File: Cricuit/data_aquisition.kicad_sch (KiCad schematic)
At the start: 45 parts, among them J1 Raspberry_Pi_2_3, SW1 SW_SPST, SW10 SW_SPST, SW2 SW_SPST, SW3 SW_SPST, SW4 SW_SPST, SW5 SW_SPST, SW6 SW_SPST, SW7 SW_SPST, SW8 SW_SPST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

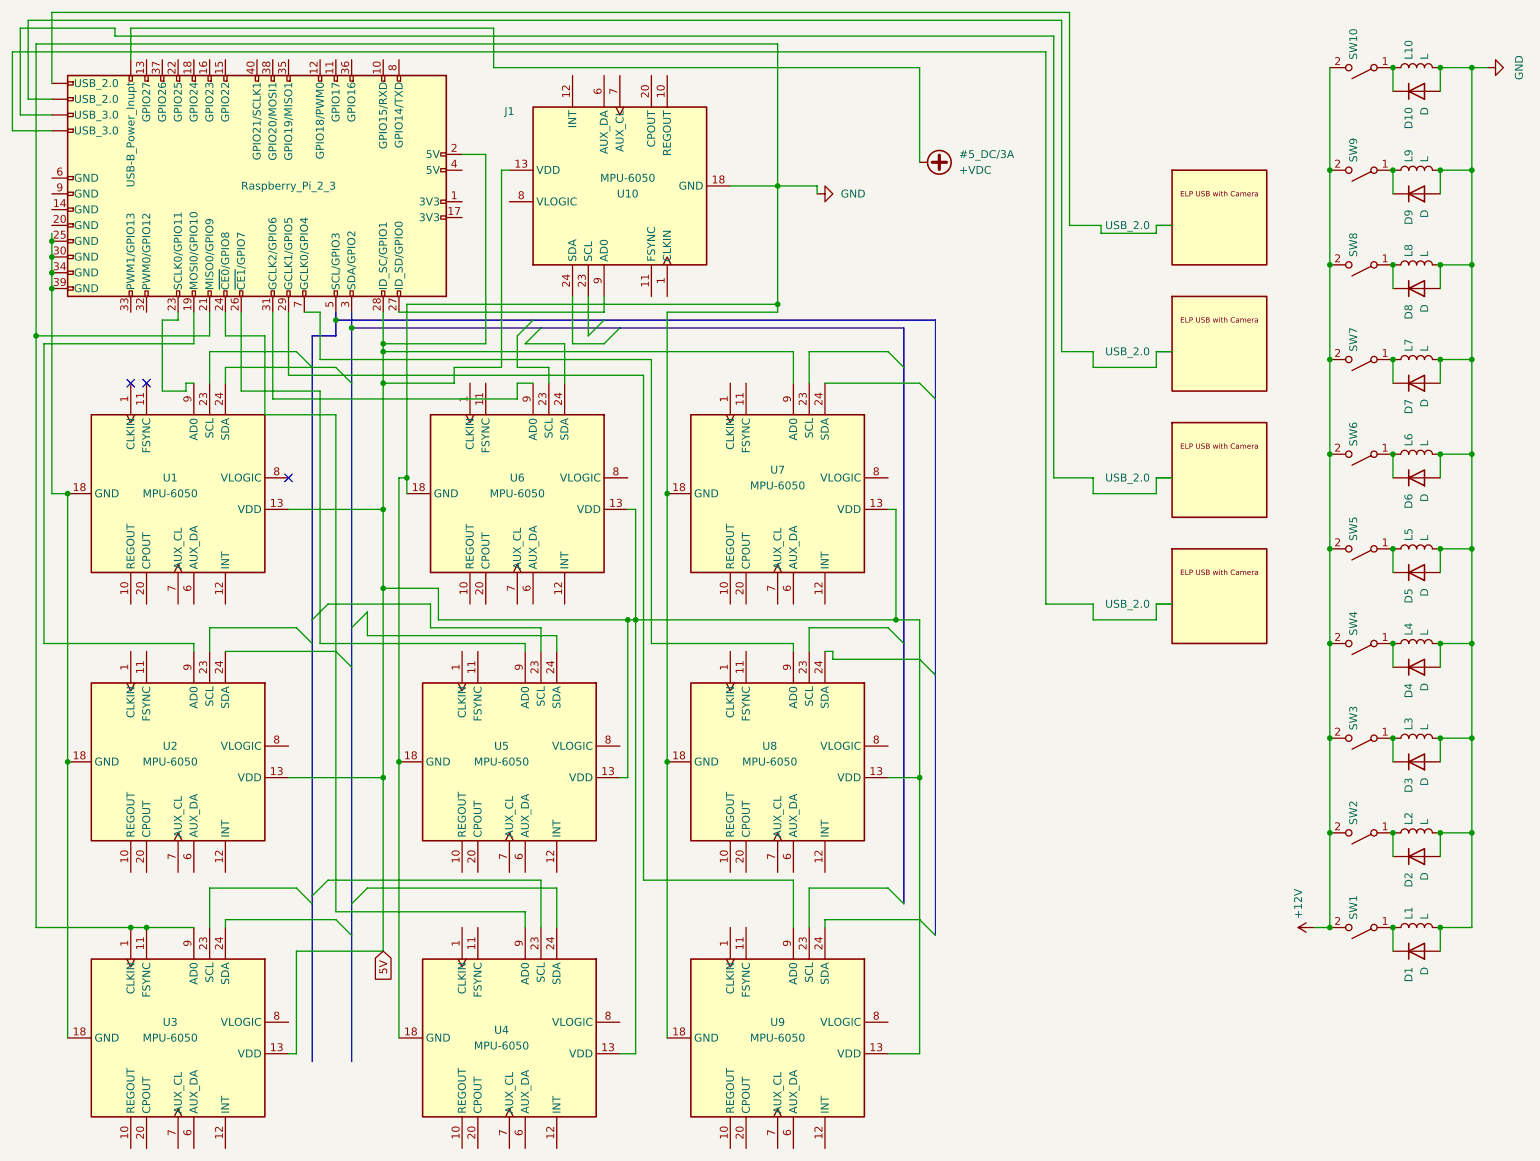
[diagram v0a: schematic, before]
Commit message: Reorganized the schematic
I chose arbitrary GPIO pins.
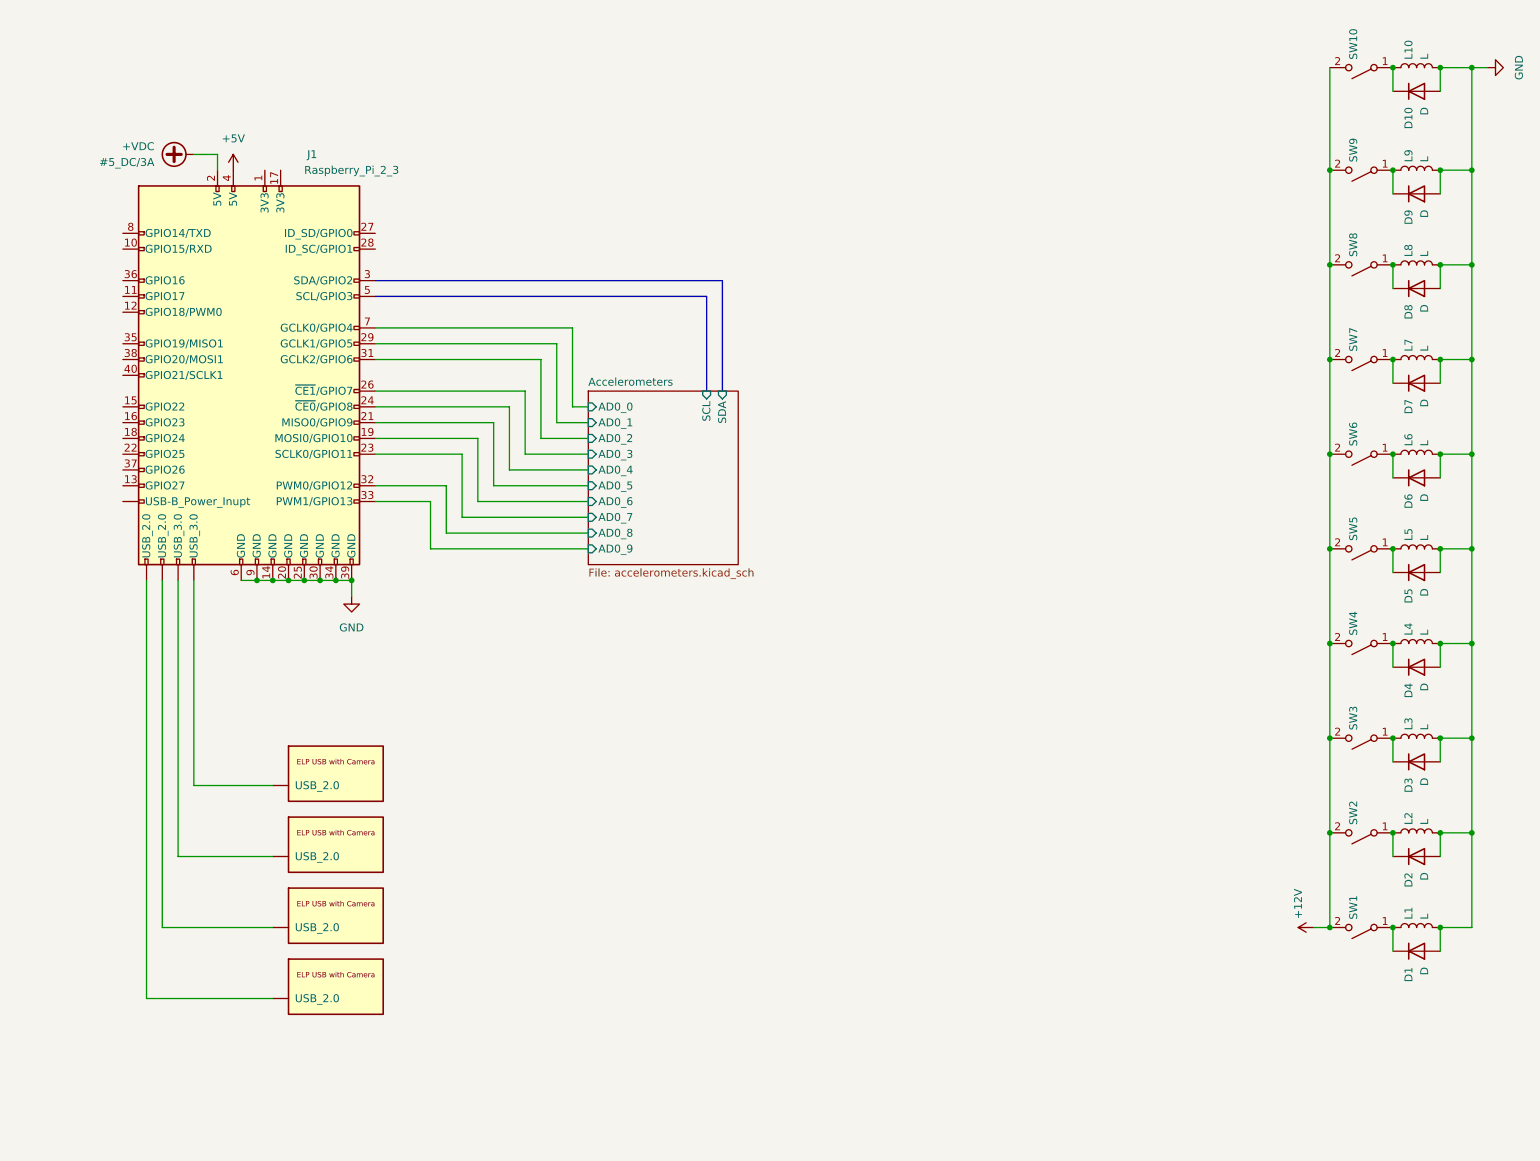
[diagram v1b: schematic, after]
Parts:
- removed U1, U10, U2, U3, U4, U5, U6, U7, U8, U9: MPU-6050, Sensor_Motion:InvenSense_QFN-24_4x4mm_P0.5mm, symbol Sensor_Motion:MPU-6050
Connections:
- net +VDC: now also J1.2 (5V); no longer J1. (USB_3.0)
- net GND: now also J1.14 (GND), J1.20 (GND), J1.25 (GND), J1.30 (GND), J1.34 (GND), J1.39 (GND), J1.6 (GND), J1.9 (GND); no longer J1.21 (MISO0/GPIO9)
- net Accelerometers/AD0_6: now reaches J1.19 (MOSI0/GPIO10)
- net Accelerometers/AD0_7: now reaches J1.23 (SCLK0/GPIO11)
- net Accelerometers/AD0_4: now reaches J1.24 (~{CE0}/GPIO8)
- net Accelerometers/AD0_3: now reaches J1.26 (~{CE1}/GPIO7)
- net Accelerometers/AD0_1: now reaches J1.29 (GCLK1/GPIO5)
- net Accelerometers/AD0_2: now reaches J1.31 (GCLK2/GPIO6)
- net Accelerometers/AD0_8: now reaches J1.32 (PWM0/GPIO12)
- net Accelerometers/AD0_9: now reaches J1.33 (PWM1/GPIO13)
- net +5V: now reaches J1.4 (5V)
- net Accelerometers/AD0_0: now reaches J1.7 (GCLK0/GPIO4)
- net 5V: no longer names the net of J1.28 (ID_SC/GPIO1)
- net 5V: no longer J1.2 (5V)
- new net Accelerometers/AD0_5: J1.21 (MISO0/GPIO9)
- no-connect marks 3 -> 0
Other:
- added sheet Accelerometers (accelerometers.kicad_sch)
- moved on the sheet: J1

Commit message: Small fix
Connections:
- net at J1. (USB_3.0): now also U14. (USB_2.0)

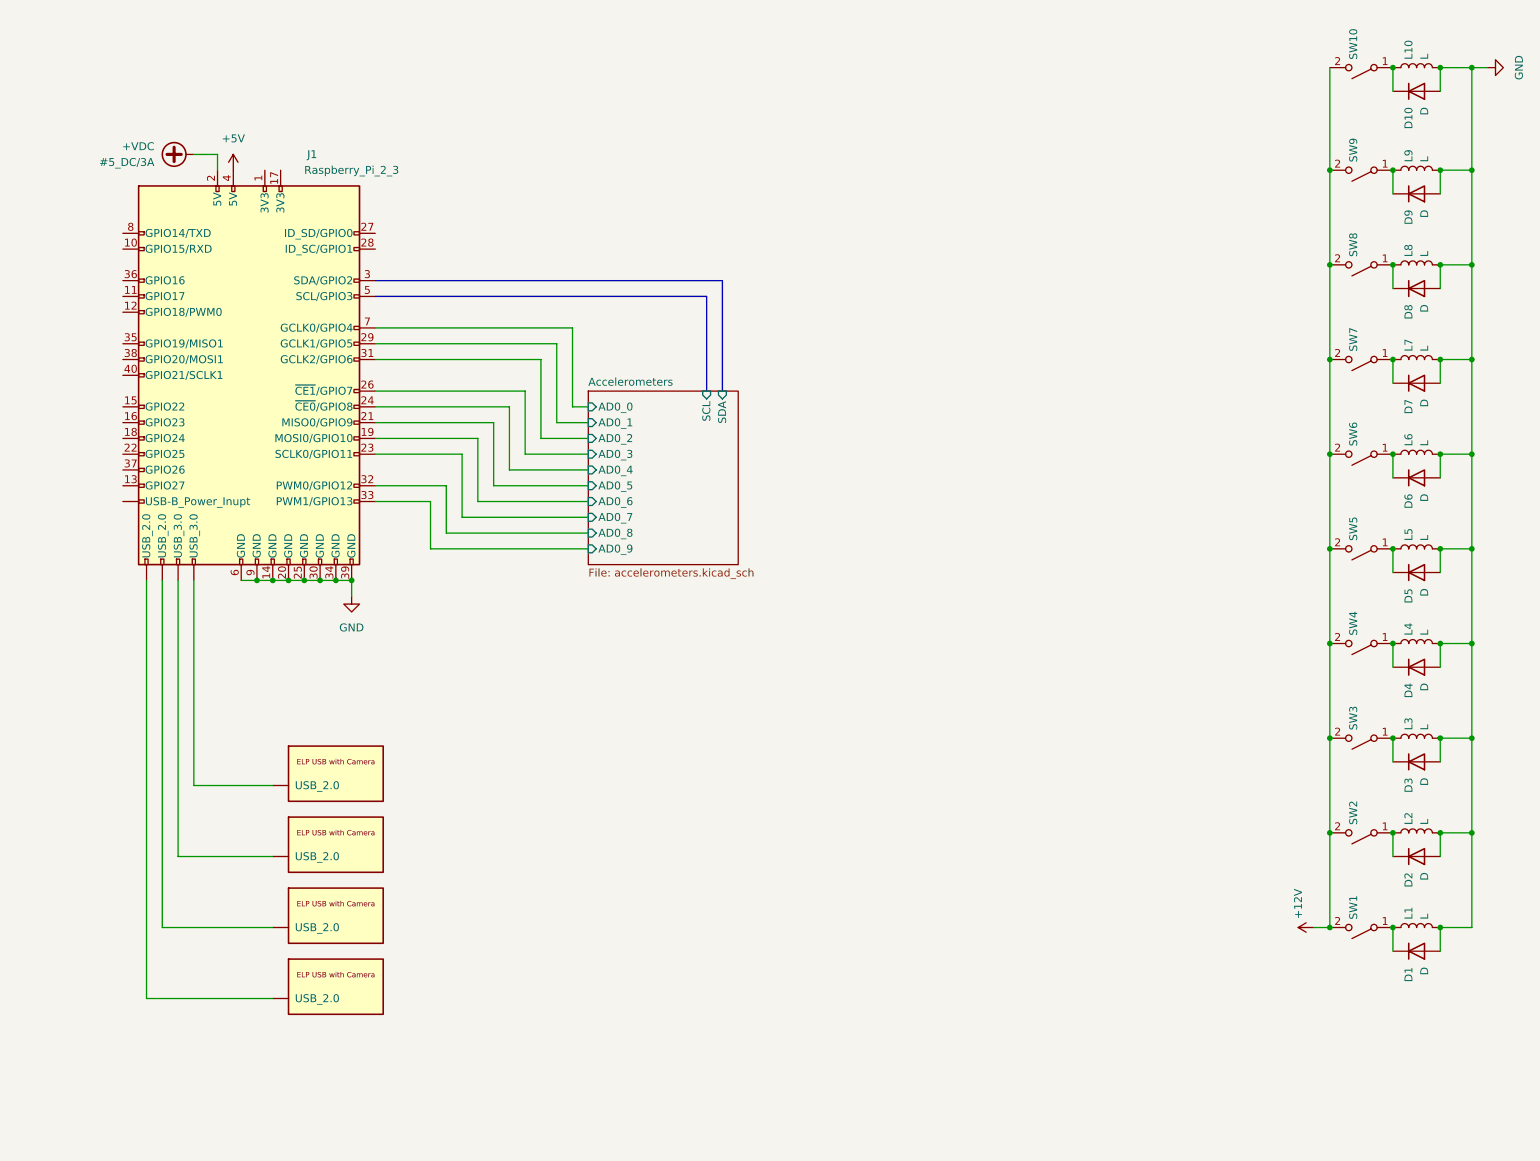
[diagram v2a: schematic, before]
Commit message: Added electromagnet subsheet
Now we have GPIO pin assignments for all components
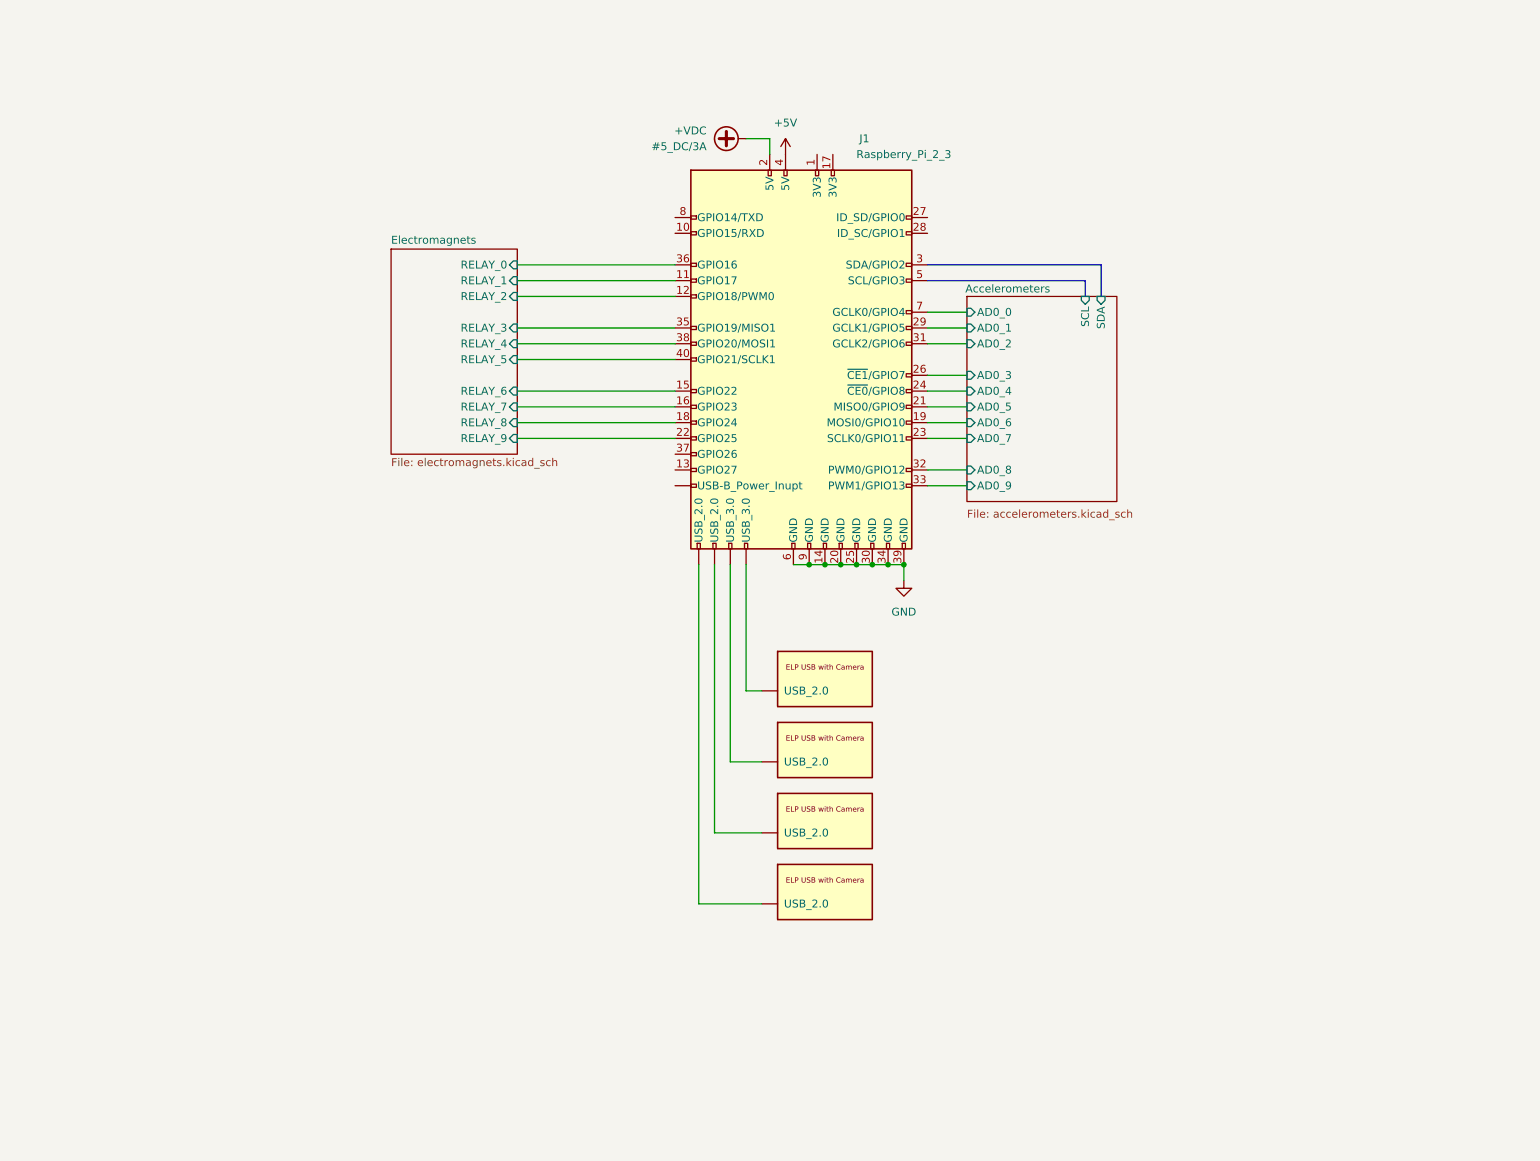
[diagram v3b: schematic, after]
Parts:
- removed D1, D10, D2, D3, D4, D5, D6, D7, D8, D9: D, symbol Device:D
- removed L1, L10, L2, L3, L4, L5, L6, L7, L8, L9: L, symbol Device:L
- removed SW1, SW10, SW2, SW3, SW4, SW5, SW6, SW7, SW8, SW9: SW_SPST, symbol Switch:SW_SPST
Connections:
- net at J1. (USB_3.0): now also U14. (USB_2.0)
- net Electromagnets/RELAY_1: now reaches J1.11 (GPIO17)
- net Electromagnets/RELAY_2: now reaches J1.12 (GPIO18/PWM0)
- net Electromagnets/RELAY_6: now reaches J1.15 (GPIO22)
- net Electromagnets/RELAY_7: now reaches J1.16 (GPIO23)
- net Electromagnets/RELAY_8: now reaches J1.18 (GPIO24)
- net Electromagnets/RELAY_9: now reaches J1.22 (GPIO25)
- net Electromagnets/RELAY_3: now reaches J1.35 (GPIO19/MISO1)
- net Electromagnets/RELAY_0: now reaches J1.36 (GPIO16)
- net Electromagnets/RELAY_4: now reaches J1.38 (GPIO20/MOSI1)
- net Electromagnets/RELAY_5: now reaches J1.40 (GPIO21/SCLK1)
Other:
- added sheet Electromagnets (electromagnets.kicad_sch)
- company: (none) -> CMD_SAT
- title: (none) -> Data Acquisition and Latching Circuits
- moved on the sheet: J1

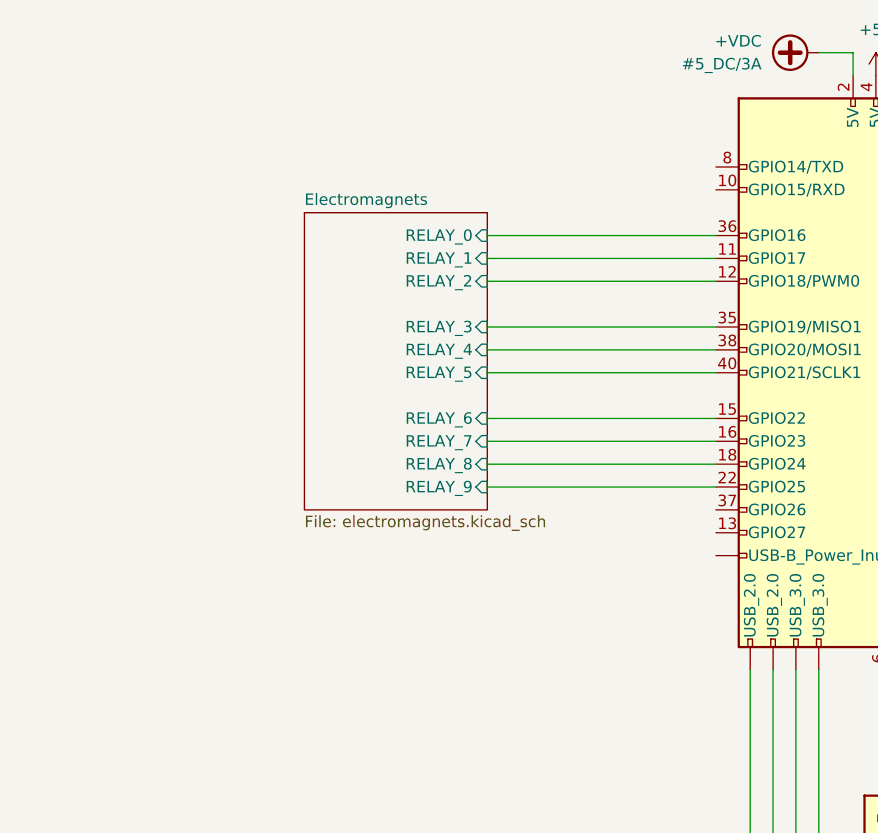
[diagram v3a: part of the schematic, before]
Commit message: even simpler datalogger
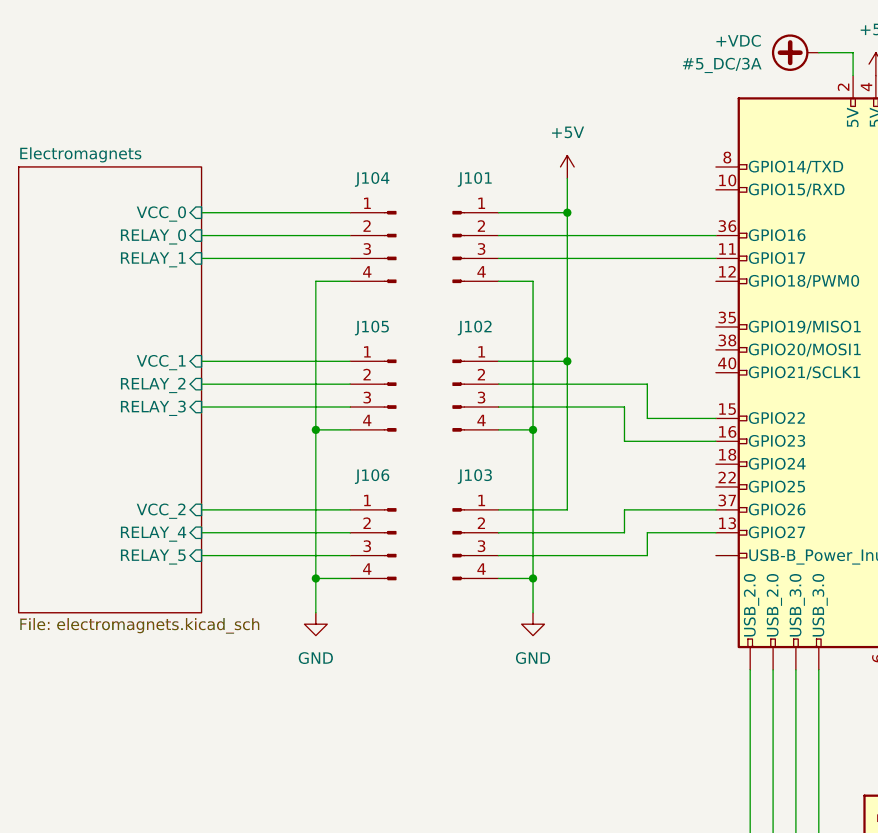
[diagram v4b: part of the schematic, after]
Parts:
- added J101, J102, J103, J104, J105, J106: Conn_01x04_Pin, symbol Connector:Conn_01x04_Pin
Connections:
- net +5V: now also J101.1 (Pin_1), J102.1 (Pin_1), J103.1 (Pin_1)
- net Electromagnets/RELAY_0: now also J104.2 (Pin_2); no longer J1.36 (GPIO16)
- net Electromagnets/RELAY_1: now also J104.3 (Pin_3); no longer J1.11 (GPIO17)
- net Electromagnets/RELAY_2: now also J105.2 (Pin_2); no longer J1.12 (GPIO18/PWM0)
- net Electromagnets/RELAY_3: now also J105.3 (Pin_3); no longer J1.35 (GPIO19/MISO1)
- net Electromagnets/RELAY_4: now also J106.2 (Pin_2); no longer J1.38 (GPIO20/MOSI1)
- net Electromagnets/RELAY_5: now also J106.3 (Pin_3); no longer J1.40 (GPIO21/SCLK1)
- net GND: now also J101.4 (Pin_4), J102.4 (Pin_4), J103.4 (Pin_4), J104.4 (Pin_4), J105.4 (Pin_4), J106.4 (Pin_4)
- net at J1. (USB_3.0): now also U14. (USB_2.0)
- net at J1.13 (GPIO27): now also J103.3 (Pin_3)
- net at J1.37 (GPIO26): now also J103.2 (Pin_2)
- net Electromagnets/RELAY_6: no longer names the net of J1.15 (GPIO22)
- net Electromagnets/RELAY_6: now also J102.2 (Pin_2)
- net Electromagnets/RELAY_7: no longer names the net of J1.16 (GPIO23)
- net Electromagnets/RELAY_7: now also J102.3 (Pin_3)
- net Electromagnets/RELAY_8: no longer names the net of J1.18 (GPIO24)
- net Electromagnets/RELAY_9: no longer names the net of J1.22 (GPIO25)
- new net: J1.11 (GPIO17), J101.3 (Pin_3)
- new net: J1.36 (GPIO16), J101.2 (Pin_2)
- new net Electromagnets/VCC_0: J104.1 (Pin_1)
- new net Electromagnets/VCC_1: J105.1 (Pin_1)
- new net Electromagnets/VCC_2: J106.1 (Pin_1)
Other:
- sheet Electromagnets ports: added VCC_0, VCC_1, VCC_2; removed RELAY_6, RELAY_7, RELAY_8, RELAY_9
